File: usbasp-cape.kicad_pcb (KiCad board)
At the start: 2 copper layers, 86.4 x 54.6 mm, 1 part, among them U1 BEAGLEBONEBLACK

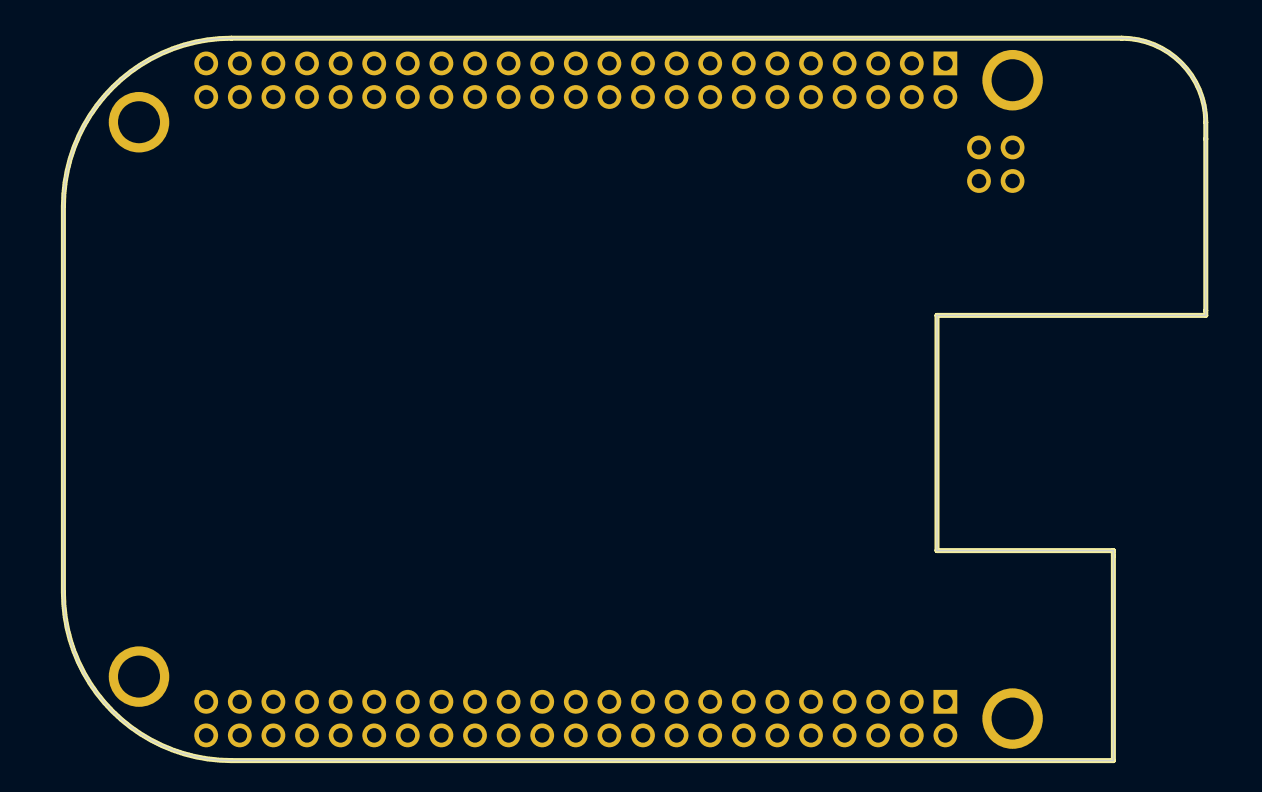
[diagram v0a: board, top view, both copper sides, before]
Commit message: pcb board routed, silkscreen not ready
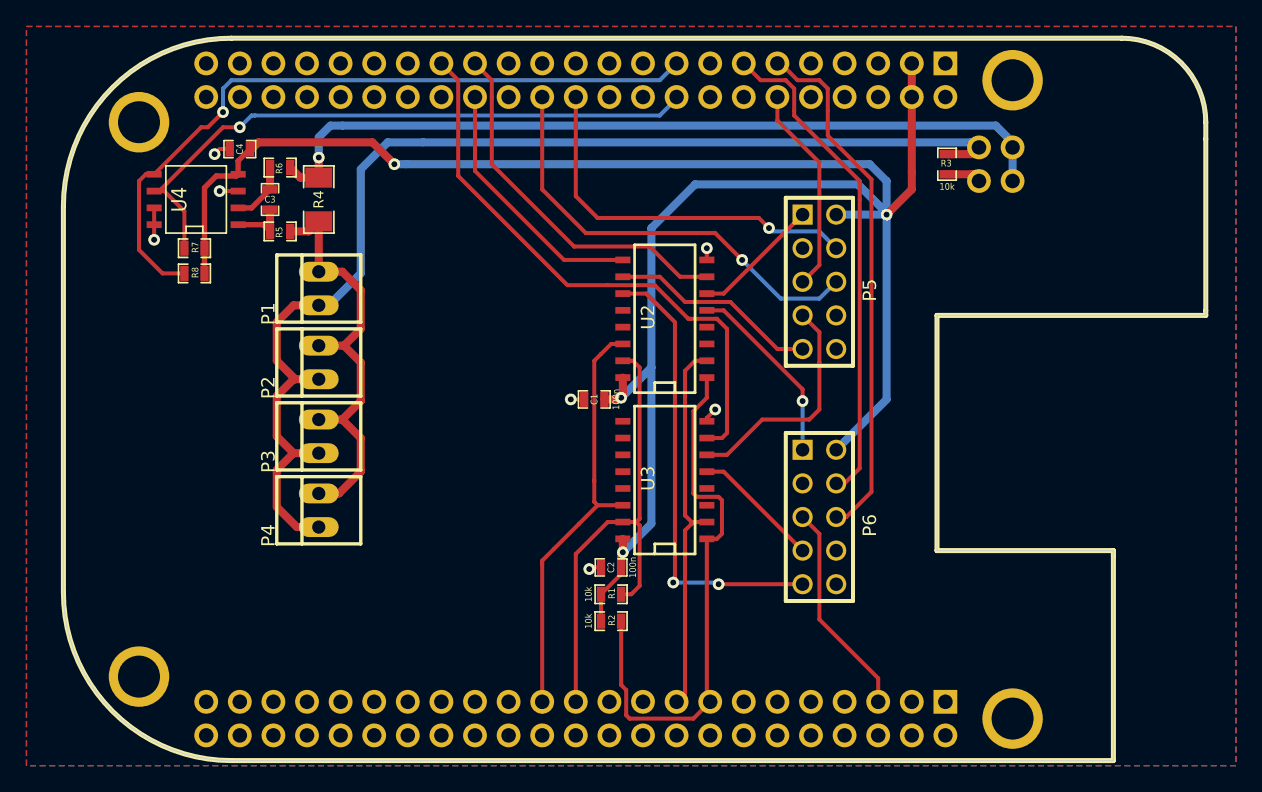
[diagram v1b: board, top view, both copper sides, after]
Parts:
- added C1: 100n, SM0603_Capa, F.Cu at (146.8, 99.1)
- added C2: 100n, SM0603_Capa, F.Cu at (148.1, 111.8)
- added C3: 100n, SM0603_Capa, F.Cu at (122.3, 83.9)
- added C4: 100n, SM0603_Capa, F.Cu at (120.0, 80.1)
- added P1: CONN_2, PINHEAD1-2, F.Cu at (126.0, 90.7)
- added P2: CONN_2, PINHEAD1-2, F.Cu at (126.0, 96.3)
- added P3: CONN_2, PINHEAD1-2, F.Cu at (126.0, 101.9)
- added P4: CONN_2, PINHEAD1-2, F.Cu at (126.0, 107.4)
- added P5: CONN_5X2, PIN_ARRAY_5x2, F.Cu at (163.8, 90.2)
- added P6: CONN_5X2, PIN_ARRAY_5x2, F.Cu at (163.8, 108.0)
- added R1: 10k, SM0603_Resistor, F.Cu at (148.1, 113.8)
- added R2: 10k, SM0603_Resistor, F.Cu at (148.1, 115.8)
- added R3: 10k, SM0603_Resistor, F.Cu at (173.5, 81.3)
- added R4: 0.2R, SM1206, F.Cu at (126.0, 83.9)
- added R5: 10k, SM0603_Resistor, F.Cu at (123.1, 86.4)
- added R6: 10k, SM0603_Resistor, F.Cu at (123.1, 81.5)
- added R7: 3.3k, SM0603_Resistor, F.Cu at (116.6, 87.6)
- added R8: 3.3k, SM0603_Resistor, F.Cu at (116.6, 89.5)
- added U2: SN74CBTLV3253, SO16N, F.Cu at (152.1, 93.0)
- added U3: SN74CBTLV3253, SO16N, F.Cu at (152.1, 105.2)
- added U4: INA219, SO8N, F.Cu at (116.7, 83.9)
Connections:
- U1 pad A1: N-0000085 (its old number) -> BAT_INA_OUT
- U1 pad A2: N-0000070 (its old number) -> BAT_INA_OUT
- U1 pad A3: N-0000067 (its old number) -> BAT_MINUS
- U1 pad B1: N-0000072 (its old number) -> GND
- U1 pad B15: N-0000011 -> 1OE
- U1 pad B17: N-0000043 (its old number) -> S1
- U1 pad B2: N-0000069 (its old number) -> GND
- U1 pad B23: N-0000037 (its old number) -> 2OE
- U1 pad B25: N-000009 -> S0
- U1 pad B5: N-0000049 (its old number) -> RST2
- U1 pad C1: N-0000071 (its old number) -> GND
- U1 pad C11: N-0000090 -> UART4_RX
- U1 pad C12: N-0000082 (its old number) -> RST1
- U1 pad C13: N-0000074 (its old number) -> UART4_TX
- U1 pad C17: N-0000042 (its old number) -> I2C1_SCL
- U1 pad C18: N-0000036 (its old number) -> I2C1_SDA
- U1 pad C2: N-0000068 (its old number) -> GND
- U1 pad C24: N-0000016 -> UART1_TX
- U1 pad C26: N-0000048 (its old number) -> UART1_RX
- U1 pad C27: N-0000040 (its old number) -> TARGET_RST
- U1 pad C28: N-0000034 (its old number) -> SPI1_CS0
- U1 pad C29: N-0000028 (its old number) -> SPI1_MOSI
- U1 pad C3: N-0000065 (its old number) -> 3V3
- U1 pad C30: N-0000094 -> SPI1_MISO
- U1 pad C31: N-0000086 (its old number) -> SPI1_SCLK
- U1 pad C4: N-0000062 (its old number) -> 3V3
- U1 pad C43: N-0000020 (its old number) -> GND
- U1 pad C44: N-0000012 -> GND
- U1 pad C45: N-000004 -> GND
- U1 pad C46: N-0000044 (its old number) -> GND
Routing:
- net 3V3: track 0.00 -> 157.9 mm, vias 0 -> 4
- net BAT_MINUS: track 0.00 -> 89.9 mm
- net BAT_INA_OUT: track 0.00 -> 61.9 mm, vias 0 -> 1
- net I2C1_SCL: track 0.00 -> 54.7 mm, vias 0 -> 1
- net I2C1_SDA: track 0.00 -> 48.2 mm, vias 0 -> 1
- net SPI1_SCLK: track 0.00 -> 43.7 mm
- net 1OE: track 0.00 -> 42.1 mm
- net UART4_RX: track 0.00 -> 39.9 mm
- net UART4_TX: track 0.00 -> 37.6 mm
- net 2OE: track 0.00 -> 36.6 mm
- net MISO2: track 0.00 -> 34.4 mm, vias 0 -> 2
- net BAT_PLUS: track 0.00 -> 33.5 mm
- net UART1_RX: track 0.00 -> 33.2 mm, vias 0 -> 1
- net S0: track 0.00 -> 33.0 mm
- net S1: track 0.00 -> 29.3 mm
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- added copper zone on B.Cu, net GND
- added copper zone on F.Cu, net GND
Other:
- net class Default: clearance 0.254 -> 0.2032
- rule trace_clearance: 0.254 -> 0.2032

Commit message: add logos to silkscreen, add polygons
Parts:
- added G***: OSHW-logo_silkscreen-front_20mm, OSHW-logo_silkscreen-front_20mm, F.Cu at (138.6, 99.1)
- added VAL: REF, logo_d_tag, F.Cu at (185.0, 83.6)
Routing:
- net GND: track 9.11 -> 16.2 mm, vias 7 -> 9
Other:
- board text added: "+"
- board text added: "PORT 1"
- board text added: "PORT 2"
- board text added: "USBASP CAPE"
- board text added: "version: A"
